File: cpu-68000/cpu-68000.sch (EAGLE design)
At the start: 101 parts, among them IC201 AS6C4008, IC202 AS6C4008, IC203 39SF040, IC204 39SF040, IC301 XR68C681, IC302 DS1244Y, IC303 MAX232, IC401 GAL22V10, IC402 GAL22V10, IC403 74HC14D, IC404 LM3724, IC405 74HC175D, J201 POWER_JACK, Q301 3.6864 MHz

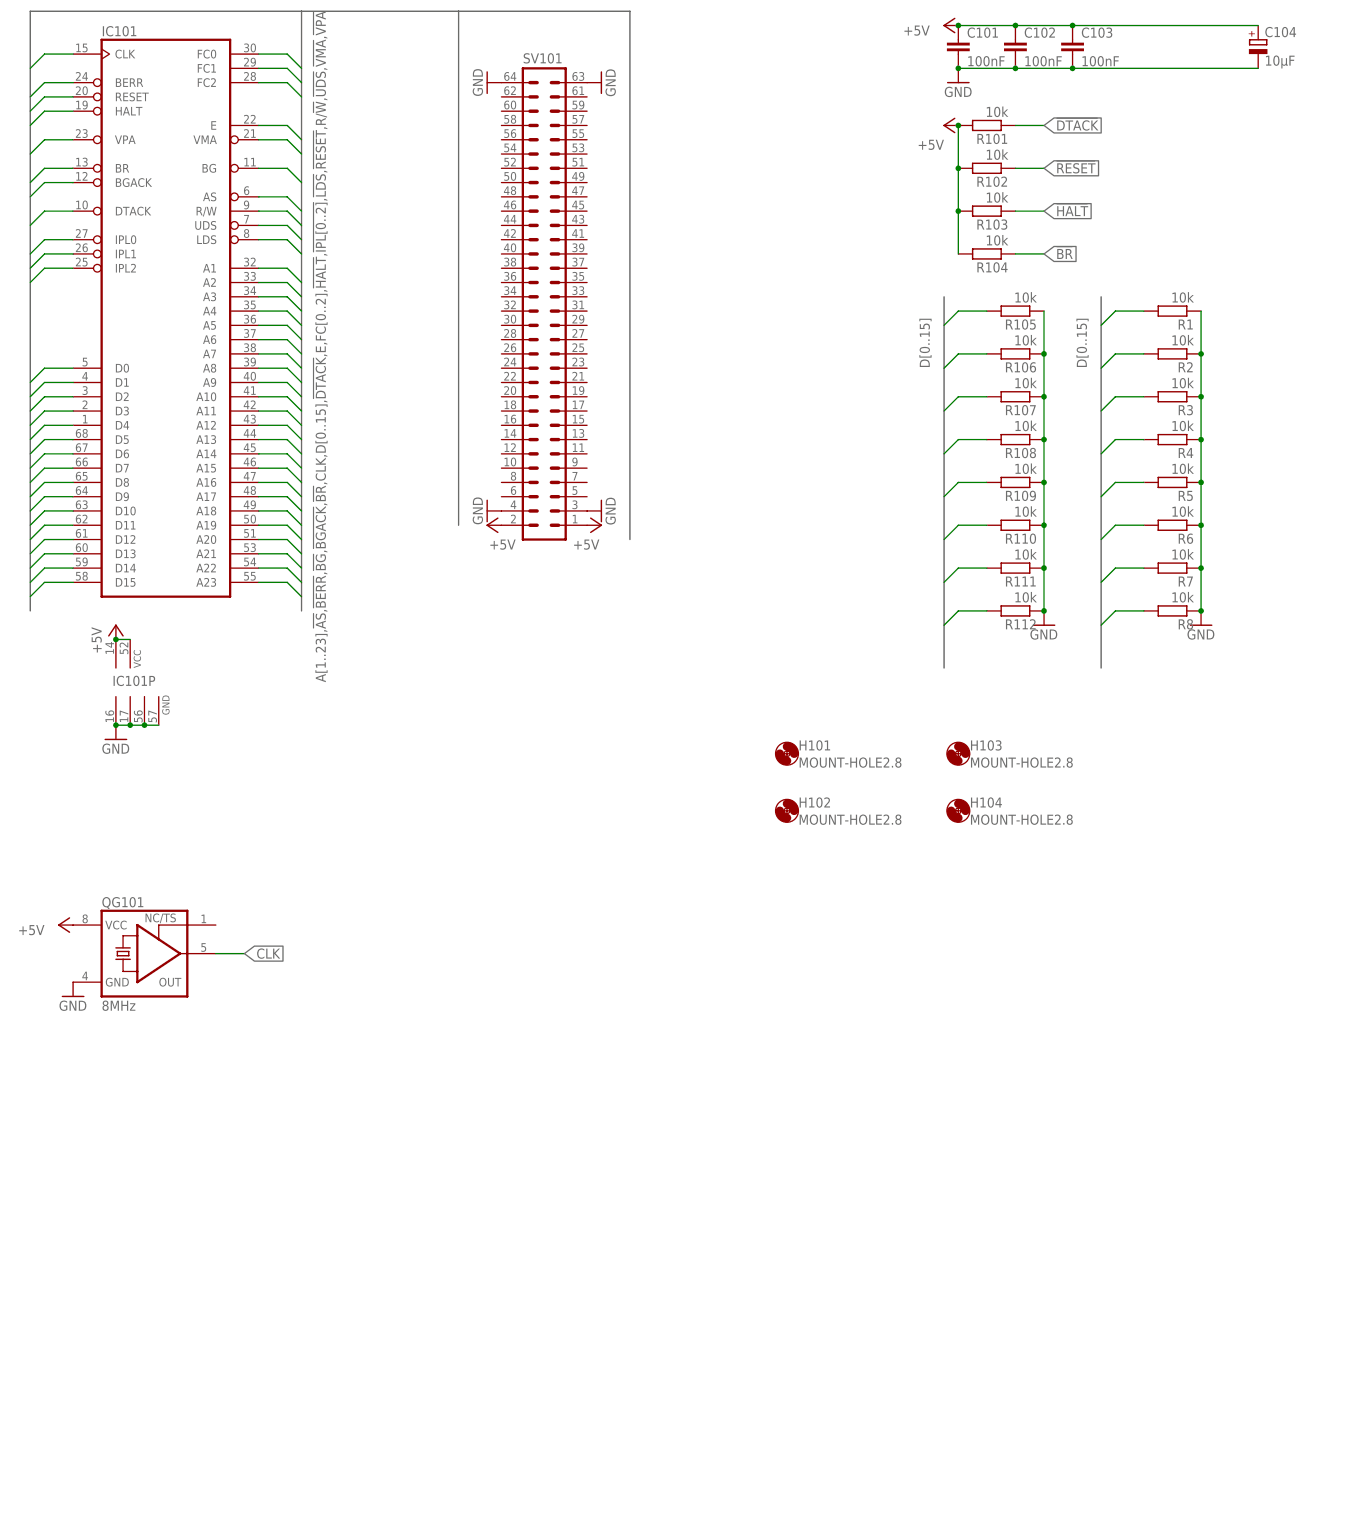
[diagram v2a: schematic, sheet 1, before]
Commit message: Finished routing expansion connector for 68000 board
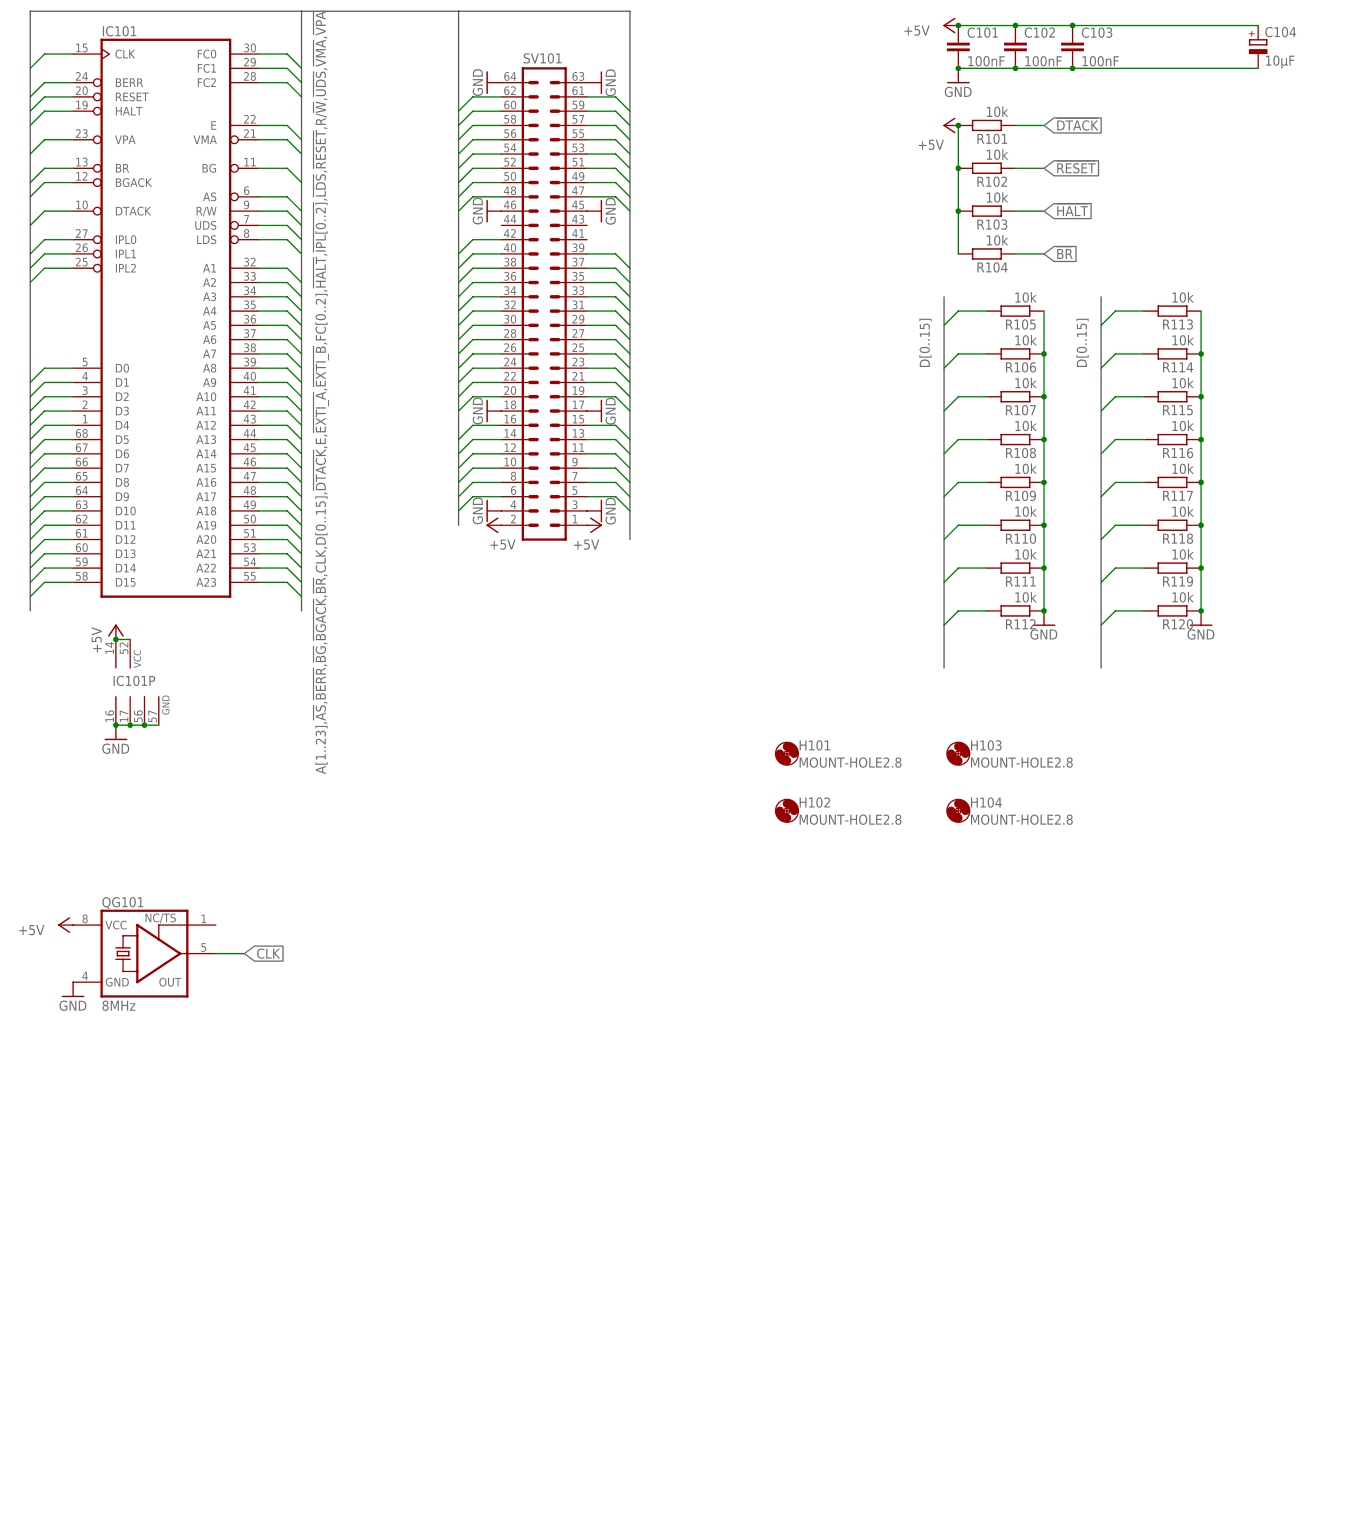
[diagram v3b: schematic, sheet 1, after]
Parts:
- added R403, R404: 10k, rcl:R-EU_R2012
- renumbered R1 to R113, R2 to R114, R3 to R115, R4 to R116, R5 to R117, R6 to R118, R7 to R119, R8 to R120
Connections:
- net !AS: now also SV101.13
- net !BG: now also SV101.9
- net !BGACK: now also SV101.8
- net !BR: now also SV101.7
- net !DTACK: now also SV101.10
- net !EXTI_A: now also R403.1, SV101.16
- net !EXTI_B: now also R404.1, SV101.15
- net !HALT: now also SV101.5
- net !LDS: now also SV101.11
- net !RESET: now also SV101.6
- net !UDS: now also SV101.14
- net +5V: now also R403.2, R404.2
- net A1: now also SV101.20
- net A10: now also SV101.27
- net A11: now also SV101.30
- net A12: now also SV101.29
- net A13: now also SV101.31
- net A14: now also SV101.32
- net A15: now also SV101.33
- net A16: now also SV101.34
- net A17: now also SV101.36
- net A18: now also SV101.35
- net A19: now also SV101.38
- net A2: now also SV101.22
- net A20: now also SV101.37
- net A21: now also SV101.40
- net A22: now also SV101.39
- net A23: now also SV101.42
- net A3: now also SV101.19
- net A4: now also SV101.24
- net A5: now also SV101.21
- net A6: now also SV101.23
- net A7: now also SV101.26
- net A8: now also SV101.25
- net A9: now also SV101.28
- net D0: now also SV101.62
- net D1: now also SV101.60
- net D10: now also SV101.61
- net D11: now also SV101.55
- net D12: now also SV101.53
- net D13: now also SV101.51
- net D14: now also SV101.49
- net D15: now also SV101.47
- net D2: now also SV101.58
- net D3: now also SV101.56
- net D4: now also SV101.54
- net D5: now also SV101.52
- net D6: now also SV101.50
- net D7: now also SV101.48
- net D8: now also SV101.57
- net D9: now also SV101.59
- net GND: now also SV101.17, SV101.18, SV101.45, SV101.46, X301.G1, X301.G2
- net R/!W!: now also SV101.12

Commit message: Enlarged 68000 board to 100x160mm (Eurocard size) Moved high/low words sections to accomodate ZIF sockets better
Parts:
- added C1: 1µF, rcl:C-EUC0805
- added C105: 100nF, rcl:C-EUC0805
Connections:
- removed net N$22: IC402.IN11
- removed net N$23: IC402.IN13
- new net !ADDR_GOOD: IC401.IO21, IC402.IN11
- net !BERR_TIMER_CLR: now also IC405A.D1
- net !DTACK: now also IC402.IO17; no longer IC401.IO21
- net +5V: now also C1.1, C105.1; no longer IC405A.D1
- net GND: now also C1.2, C105.2, SV101.41, SV101.43, SV101.44
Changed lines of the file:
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@@
 <attribute name="MOUSER" value="710-885012207072"/>
 </part>
-<part name="P+408" library="supply1" library_urn="urn:adsk.eagle:library:371" deviceset="+5V" device=""/>
 <part name="IC404" library="68komputer" deviceset="LM3724" device="" package3d_urn="urn:adsk.eagle:package:16456/2" value="LM3724"/>
 <part name="GND408" library="supply1" library_urn="urn:adsk.eagle:library:371" deviceset="GND" device=""/>
@@
 <part name="GND3" library="supply1" library_urn="urn:adsk.eagle:library:371" deviceset="GND" device=""/>
 <part name="GND4" library="supply1" library_urn="urn:adsk.eagle:library:371" deviceset="GND" device=""/>
+<part name="C105" library="rcl" library_urn="urn:adsk.eagle:library:334" deviceset="C-EU" device="C0805" package3d_urn="urn:adsk.eagle:package:23617/2" value="100nF">
+<attribute name="MOUSER" value="710-885012207072"/>
+</part>
+<part name="P+1" library="supply1" library_urn="urn:adsk.eagle:library:371" deviceset="+5V" device=""/>
+<part name="GND5" library="supply1" library_urn="urn:adsk.eagle:library:371" deviceset="GND" device=""/>
+<part name="C1" library="rcl" library_urn="urn:adsk.eagle:library:334" deviceset="C-EU" device="C0805" package3d_urn="urn:adsk.eagle:package:23617/2" value="1µF">
+<attribute name="MOUSER" value=" 710-885012207078"/>
+</part>
 </parts>
 <sheets>
@@
 <attribute name="VALUE" x="93.98" y="114.3" size="1.778" layer="96" rot="R270"/>
 </instance>
+<instance part="C105" gate="G$1" x="106.68" y="78.74" smashed="yes" rot="R270">
+<attribute name="MOUSER" x="106.68" y="78.74" size="1.27" layer="96" rot="R270" align="top-center" display="off"/>
+<attribute name="NAME" x="107.061" y="77.216" size="1.778" layer="95" rot="R270"/>
+<attribute name="VALUE" x="101.981" y="77.216" size="1.778" layer="96" rot="R270"/>
+</instance>
+<instance part="P+1" gate="1" x="111.76" y="78.74" smashed="yes" rot="MR90">
+<attribute name="VALUE" x="114.3" y="78.74" size="1.778" layer="96" rot="MR180"/>
+</instance>
+<instance part="GND5" gate="1" x="99.06" y="78.74" smashed="yes" rot="R270">
+<attribute name="VALUE" x="96.52" y="81.28" size="1.778" layer="96" rot="R270"/>
+</instance>
+<instance part="C1" gate="G$1" x="106.68" y="68.58" smashed="yes" rot="R270">
+<attribute name="MOUSER" x="106.68" y="68.58" size="1.27" layer="96" rot="R270" align="top-center" display="off"/>
+<attribute name="NAME" x="107.061" y="67.056" size="1.778" layer="95" rot="R270"/>
+<attribute name="VALUE" x="101.981" y="67.056" size="1.778" layer="96" rot="R270"/>
+</instance>
 </instances>
 <busses>
@@
 <junction x="180.34" y="147.32"/>
 </segment>
+<segment>
+<pinref part="C105" gate="G$1" pin="1"/>
+<pinref part="P+1" gate="1" pin="+5V"/>
+<pinref part="C1" gate="G$1" pin="1"/>
+<wire x1="109.22" y1="68.58" x2="109.22" y2="78.74" width="0.1524" layer="91"/>
+<junction x="109.22" y="78.74"/>
+</segment>
 </net>
 <net name="GND" class="0">
@@
 <pinref part="SV101" gate="1" pin="45"/>
 <pinref part="GND1" gate="1" pin="GND"/>
+<pinref part="SV101" gate="1" pin="41"/>
+<wire x1="114.3" y1="147.32" x2="114.3" y2="144.78" width="0.1524" layer="91"/>
+<junction x="114.3" y="147.32"/>
+<pinref part="SV101" gate="1" pin="43"/>
+<wire x1="114.3" y1="144.78" x2="114.3" y2="142.24" width="0.1524" layer="91"/>
+<junction x="114.3" y="144.78"/>
 </segment>
 <segment>
 <pinref part="SV101" gate="1" pin="46"/>
 <pinref part="GND2" gate="1" pin="GND"/>
+<pinref part="SV101" gate="1" pin="44"/>
+<wire x1="99.06" y1="144.78" x2="99.06" y2="147.32" width="0.1524" layer="91"/>
+<junction x="99.06" y="147.32"/>
 </segment>
 <segment>
@@
 <pinref part="GND4" gate="1" pin="GND"/>
 </segment>
+<segment>
+<pinref part="C105" gate="G$1" pin="2"/>
+<pinref part="GND5" gate="1" pin="GND"/>
+<pinref part="C1" gate="G$1" pin="2"/>
+<wire x1="101.6" y1="68.58" x2="101.6" y2="78.74" width="0.1524" layer="91"/>
+<junction x="101.6" y="78.74"/>
+</segment>
 </net>
 <net name="CLK" class="0">
@@
 <attribute name="VALUE" x="174.244" y="173.101" size="1.778" layer="96"/>
 </instance>
-<instance part="P+408" gate="1" x="198.12" y="139.7" smashed="yes" rot="R90">
-<attribute name="VALUE" x="195.58" y="139.7" size="1.778" layer="96" rot="R270"/>
-</instance>
 <instance part="IC404" gate="G$1" x="170.18" y="101.6" smashed="yes" rot="MR0">
 <attribute name="NAME" x="170.18" y="101.6" size="1.778" layer="95" rot="MR0"/>
@@
 </segment>
 <segment>
-<pinref part="IC405" gate="A" pin="D1"/>
-<pinref part="P+408" gate="1" pin="+5V"/>
-</segment>
-<segment>
 <pinref part="IC404" gate="G$1" pin="VCC"/>
 <pinref part="P+407" gate="1" pin="+5V"/>
@@
 <label x="78.74" y="109.22" size="1.778" layer="95" xref="yes"/>
 </segment>
+<segment>
+<pinref part="IC405" gate="A" pin="D1"/>
+<wire x1="200.66" y1="139.7" x2="195.58" y2="139.7" width="0.1524" layer="91"/>
+<label x="195.58" y="139.7" size="1.778" layer="95" rot="R180" xref="yes"/>
+</segment>
 </net>
 <net name="E" class="0">
@@
 </segment>
 </net>
-<net name="N$22" class="0">
-<segment>
-<pinref part="IC402" gate="G$1" pin="IN11"/>
-<wire x1="35.56" y1="81.28" x2="40.64" y2="81.28" width="0.1524" layer="91"/>
-</segment>
-</net>
-<net name="N$23" class="0">
-<segment>
-<pinref part="IC402" gate="G$1" pin="IN13"/>
-<wire x1="35.56" y1="78.74" x2="40.64" y2="78.74" width="0.1524" layer="91"/>
-</segment>
-</net>
 <net name="!NMI" class="0">
 <segment>
@@
 <net name="!DTACK" class="0">
 <segment>
-<pinref part="IC401" gate="G$1" pin="IO21"/>
-<wire x1="73.66" y1="157.48" x2="78.74" y2="157.48" width="0.1524" layer="91"/>
-<label x="78.74" y="157.48" size="1.778" layer="95" xref="yes"/>
+<pinref part="IC402" gate="G$1" pin="IO17"/>
+<wire x1="73.66" y1="101.6" x2="78.74" y2="101.6" width="0.1524" layer="91"/>
+<label x="78.74" y="101.6" size="1.778" layer="95" xref="yes"/>
 </segment>
 </net>
@@
 </segment>
 </net>
+<net name="!ADDR_GOOD" class="0">
+<segment>
+<pinref part="IC401" gate="G$1" pin="IO21"/>
+<wire x1="73.66" y1="157.48" x2="78.74" y2="157.48" width="0.1524" layer="91"/>
+<label x="78.74" y="157.48" size="1.778" layer="95" xref="yes"/>
+</segment>
+<segment>
+<pinref part="IC402" gate="G$1" pin="IN11"/>
+<wire x1="40.64" y1="81.28" x2="35.56" y2="81.28" width="0.1524" layer="91"/>
+<label x="35.56" y="81.28" size="1.778" layer="95" rot="R180" xref="yes"/>
+</segment>
+</net>

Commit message: CPU board: 	- Clean up some traces
IO board:
	- Started work on super IO board
	- UARTs, parallel port, PS/2 keyboard/mouse interface, I2C

2MB RAM Expansion:
	- Added some address decoding
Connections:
- new net !EXT_ID: IC301.OP6, SV101.41
- net GND: no longer SV101.41
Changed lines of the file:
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@@
 <?xml version="1.0" encoding="utf-8"?>
 <!DOCTYPE eagle SYSTEM "eagle.dtd">
-<eagle version="9.4.2">
+<eagle version="9.5.2">
 <drawing>
 <settings>
@@
 </instances>
 <busses>
-<bus name="A[1..23],!AS,!BERR,!BG,!BGACK,!BR,CLK,D[0..15],!DTACK,E,!EXTI_A,!EXTI_B,FC[0..2],!HALT,!IPL[0..2],!LDS,!RESET,R/!W!,!UDS,!VMA,!VPA">
+<bus name="A[1..23],!AS,!BERR,!BG,!BGACK,!BR,CLK,D[0..15],!DTACK,E,!EXTI_A,!EXTI_B,!EXT_ID,FC[0..2],!HALT,!IPL[0..2],!LDS,!RESET,R/!W!,!UDS,!VMA,!VPA">
 <segment>
 <wire x1="15.24" y1="76.2" x2="15.24" y2="182.88" width="0.762" layer="92"/>
@@
 <pinref part="SV101" gate="1" pin="45"/>
 <pinref part="GND1" gate="1" pin="GND"/>
-<pinref part="SV101" gate="1" pin="41"/>
 <wire x1="114.3" y1="147.32" x2="114.3" y2="144.78" width="0.1524" layer="91"/>
 <junction x="114.3" y="147.32"/>
 <pinref part="SV101" gate="1" pin="43"/>
-<wire x1="114.3" y1="144.78" x2="114.3" y2="142.24" width="0.1524" layer="91"/>
-<junction x="114.3" y="144.78"/>
 </segment>
 <segment>
@@
 </segment>
 </net>
+<net name="!EXT_ID" class="0">
+<segment>
+<pinref part="SV101" gate="1" pin="41"/>
+<wire x1="114.3" y1="142.24" x2="119.38" y2="142.24" width="0.1524" layer="91"/>
+<wire x1="119.38" y1="142.24" x2="121.92" y2="139.7" width="0.1524" layer="91"/>
+</segment>
+</net>
 </nets>
 </sheet>
@@
 </instances>
 <busses>
-<bus name="!68681_CS,!68681_IRQ,68681_X[1..2],A[1..23],!A_CTS,!A_RTS,A_RX,A_TX,!B_CTS,!B_RTS,B_RX,B_TX,CONF[0..3],D[0..15],!DTACK,!LOE,!LWE,REMAP,!RESET,!RTC_CS,STATUS[0..2]">
+<bus name="!68681_CS,!68681_IRQ,68681_X[1..2],A[1..23],!A_CTS,!A_RTS,A_RX,A_TX,!B_CTS,!B_RTS,B_RX,B_TX,CONF[0..3],D[0..15],!DTACK,!EXT_ID,!LOE,!LWE,REMAP,!RESET,!RTC_CS,STATUS[0..2]">
 <segment>
 <wire x1="22.86" y1="177.8" x2="68.58" y2="177.8" width="0.762" layer="92"/>
@@
 </segment>
 </net>
+<net name="!EXT_ID" class="0">
+<segment>
+<pinref part="IC301" gate="G$1" pin="OP6"/>
+<wire x1="60.96" y1="137.16" x2="66.04" y2="137.16" width="0.1524" layer="91"/>
+<wire x1="66.04" y1="137.16" x2="68.58" y2="134.62" width="0.1524" layer="91"/>
+</segment>
+</net>
